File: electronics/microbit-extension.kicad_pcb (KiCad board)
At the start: 2 copper layers, 55.9 x 63.5 mm, 29 parts, among them J1 microbit_edge_connector, SW1 SW_DIP_x01, SW2 SW_DIP_x01, SW3 SW_DIP_x01, SW4 SW_DIP_x01, U1 LD1117S33CTR

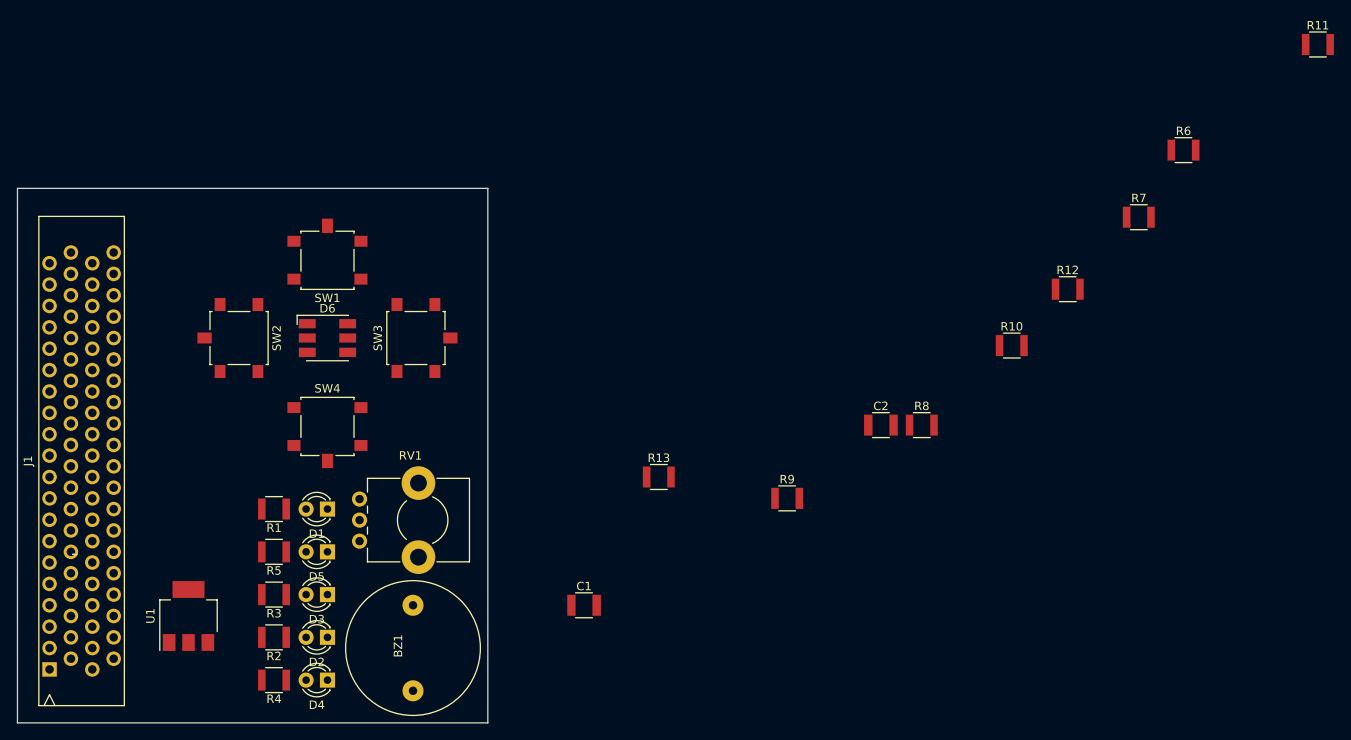
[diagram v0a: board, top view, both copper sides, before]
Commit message: need to redo and check the footprint association
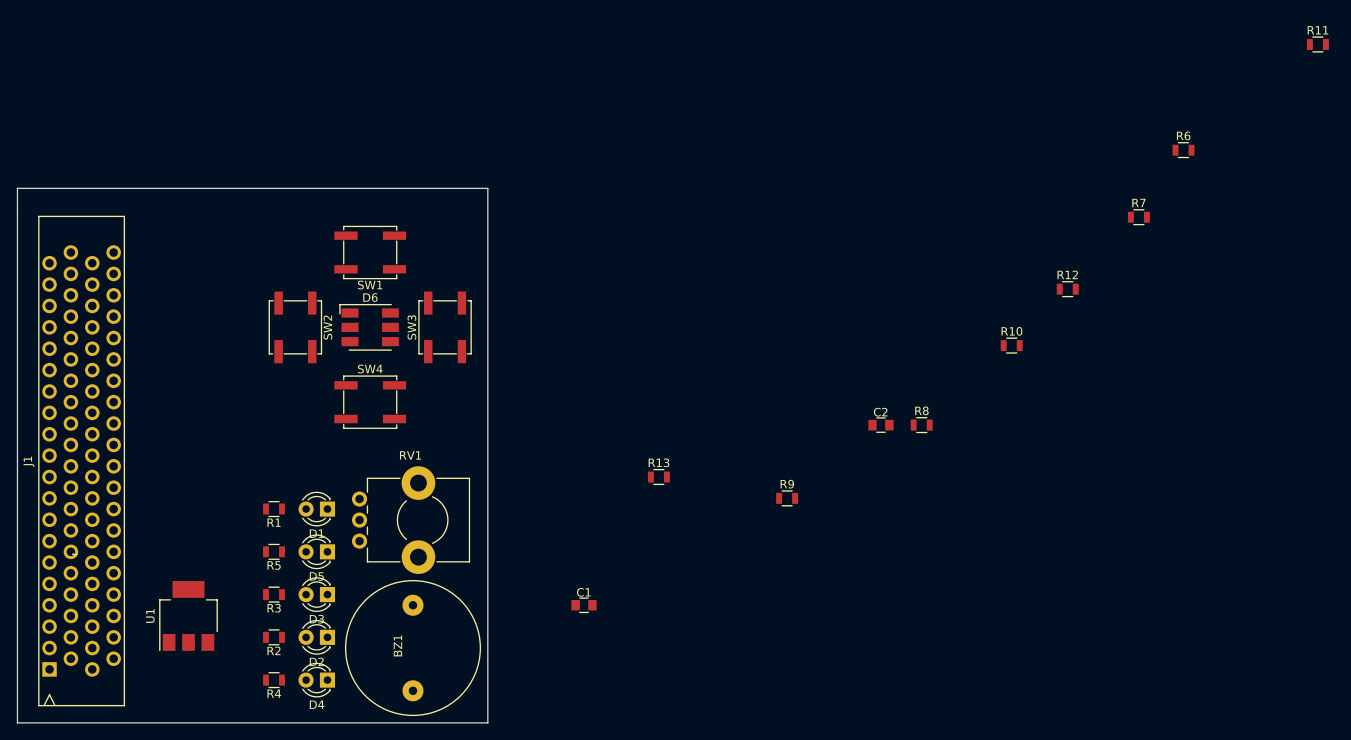
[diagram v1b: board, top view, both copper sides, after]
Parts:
- C1, C2: footprint Capacitors_SMD:C_1210 -> Capacitors_SMD:C_0805
- R1, R10, R11, R12, R13, R2, R3, R4, R5, R6, R7, R8, R9: footprint Resistors_SMD:R_1210 -> Resistors_SMD:R_0805
- SW1, SW2, SW3, SW4: footprint Buttons_Switches_SMD:SW_SPST_B3S-1100 -> Buttons_Switches_SMD:SW_SPST_EVPBF
- moved SW2 7.73 mm to (76.2, 82.5)
- moved SW4 6.35 mm to (85.1, 91.4)
- moved D6 5.24 mm to (85.1, 82.5)
- moved SW1 5.08 mm to (85.1, 73.7)
- moved SW3 2.84 mm to (94.0, 82.5)

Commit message: more layouting
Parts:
- moved U1 53.1 mm to (116.3, 122.4)
- moved D6 14.2 mm to (70.9, 82.5)
- moved SW1 14.2 mm to (70.9, 73.7)
- moved SW2 14.2 mm to (62.0, 82.5)
- moved SW3 14.2 mm to (79.8, 82.5)
- moved SW4 14.2 mm to (70.9, 91.4)
- moved D1 13.3 mm to (66.8, 103.0)
- moved D2 13.3 mm to (66.8, 118.2)
- moved D3 13.3 mm to (66.8, 113.2)
- moved D4 13.3 mm to (66.8, 123.3)
- moved D5 13.3 mm to (66.8, 108.1)
- moved R1 13.3 mm to (60.5, 103.0)
- moved R2 13.3 mm to (60.5, 118.2)
- moved R3 13.3 mm to (60.5, 113.2)
- moved R4 13.3 mm to (60.5, 123.3)
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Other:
- board size 55.9 x 63.5 mm -> 43.2 x 59.7 mm
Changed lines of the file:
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@@
     (links 78)
     (no_connects 78)
-    (area 43.104999 65.964999 99.135001 129.615001)
+    (area 43.739999 68.504999 87.070001 128.345001)
     (thickness 1.6)
     (drawings 5)
@@
   )
   (module Buzzers_Beepers:BUZZER (layer F.Cu)
-    (at 90.17 120.65 90)
+    (at 78.74 120.015 90)
     (fp_text reference BZ1 (at 0.24892 -1.75006 90) (layer F.SilkS)
       (effects (font (size 1 1) (thickness 0.15)))
@@
   )
   (module LEDs:LED_D3.0mm (layer F.Cu)
-    (at 80.01 104.14 180)
+    (at 66.802 102.997 180)
     (descr "LED, diameter 3.0mm, 2 pins")
     (tags "LED diameter 3.0mm 2 pins")
@@
   )
   (module LEDs:LED_D3.0mm (layer F.Cu)
-    (at 80.01 119.38 180)
+    (at 66.802 118.237 180)
     (descr "LED, diameter 3.0mm, 2 pins")
     (tags "LED diameter 3.0mm 2 pins")
@@
   )
   (module LEDs:LED_D3.0mm (layer F.Cu)
-    (at 80.01 114.3 180)
+    (at 66.802 113.157 180)
     (descr "LED, diameter 3.0mm, 2 pins")
     (tags "LED diameter 3.0mm 2 pins")
@@
   )
   (module LEDs:LED_D3.0mm (layer F.Cu)
-    (at 80.01 124.46 180)
+    (at 66.802 123.317 180)
     (descr "LED, diameter 3.0mm, 2 pins")
     (tags "LED diameter 3.0mm 2 pins")
@@
   )
   (module LEDs:LED_D3.0mm (layer F.Cu)
-    (at 80.01 109.22 180)
+    (at 66.802 108.077 180)
     (descr "LED, diameter 3.0mm, 2 pins")
     (tags "LED diameter 3.0mm 2 pins")
@@
   )
   (module LEDs:LED_RGB_5050-6 (layer F.Cu)
-    (at 85.09 82.55)
+    (at 70.866 82.55)
     (descr http://cdn.sparkfun.com/datasheets/Components/LED/5060BRG4.pdf)
     (tags "RGB LED 5050-6")
@@
   )
   (module Potentiometers:Potentiometer_Alps_RK09K_Horizontal (layer F.Cu)
-    (at 83.82 107.95)
+    (at 85.09 102.235 180)
     (descr "Potentiometer, horizontally mounted, Omeg PC16PU, Omeg PC16PU, Omeg PC16PU, Vishay/Spectrol 248GJ/249GJ Single, Vishay/Spectrol 248GJ/249GJ Single, Vishay/Spectrol 248GJ/249GJ Single, Vishay/Spectrol 248GH/249GH Single, Vishay/Spectrol 148/149 Single, Vishay/Spectrol 148/149 Single, Vishay/Spectrol 148/149 Single, Vishay/Spectrol 148A/149A Single with mounting plates, Vishay/Spectrol 148/149 Double, Vishay/Spectrol 148A/149A Double with mounting plates, Piher PC-16 Single, Piher PC-16 Single, Piher PC-16 Single, Piher PC-16SV Single, Piher PC-16 Double, Piher PC-16 Triple, Piher T16H Single, Piher T16L Single, Piher T16H Double, Alps RK163 Single, Alps RK163 Double, Alps RK097 Single, Alps RK097 Double, Bourns PTV09A-2 Single with mounting sleve Single, Bourns PTV09A-1 with mounting sleve Single, Bourns PRS11S Single, Alps RK09K Single with mounting sleve Single, Alps RK09K with mounting sleve Single, http://www.alps.com/prod/info/E/HTML/Potentiometer/RotaryPotentiometers/RK09K/RK09D1130C1B.html")
     (tags "Potentiometer horizontal  Omeg PC16PU  Omeg PC16PU  Omeg PC16PU  Vishay/Spectrol 248GJ/249GJ Single  Vishay/Spectrol 248GJ/249GJ Single  Vishay/Spectrol 248GJ/249GJ Single  Vishay/Spectrol 248GH/249GH Single  Vishay/Spectrol 148/149 Single  Vishay/Spectrol 148/149 Single  Vishay/Spectrol 148/149 Single  Vishay/Spectrol 148A/149A Single with mounting plates  Vishay/Spectrol 148/149 Double  Vishay/Spectrol 148A/149A Double with mounting plates  Piher PC-16 Single  Piher PC-16 Single  Piher PC-16 Single  Piher PC-16SV Single  Piher PC-16 Double  Piher PC-16 Triple  Piher T16H Single  Piher T16L Single  Piher T16H Double  Alps RK163 Single  Alps RK163 Double  Alps RK097 Single  Alps RK097 Double  Bourns PTV09A-2 Single with mounting sleve Single  Bourns PTV09A-1 with mounting sleve Single  Bourns PRS11S Single  Alps RK09K Single with mounting sleve Single  Alps RK09K with mounting sleve Single")
-    (fp_text reference RV1 (at 6.05 -10.15) (layer F.SilkS)
-      (effects (font (size 1 1) (thickness 0.15)))
-    )
-    (fp_text value POT (at 6.05 5.15) (layer F.Fab)
+    (fp_text reference RV1 (at 6.05 -10.15 180) (layer F.SilkS)
+      (effects (font (size 1 1) (thickness 0.15)))
+    )
+    (fp_text value POT (at 6.05 5.15 180) (layer F.Fab)
       (effects (font (size 1 1) (thickness 0.15)))
     )
@@
     (fp_line (start 13.25 4.15) (end 13.25 -9.15) (layer F.CrtYd) (width 0.05))
     (fp_line (start 13.25 -9.15) (end -1.15 -9.15) (layer F.CrtYd) (width 0.05))
-    (pad 3 thru_hole circle (at 0 -5) (size 1.8 1.8) (drill 1) (layers *.Cu *.Mask)
+    (pad 3 thru_hole circle (at 0 -5 180) (size 1.8 1.8) (drill 1) (layers *.Cu *.Mask)
       (net 2 +3V3))
-    (pad 2 thru_hole circle (at 0 -2.5) (size 1.8 1.8) (drill 1) (layers *.Cu *.Mask)
+    (pad 2 thru_hole circle (at 0 -2.5 180) (size 1.8 1.8) (drill 1) (layers *.Cu *.Mask)
       (net 37 /AI0))
-    (pad 1 thru_hole circle (at 0 0) (size 1.8 1.8) (drill 1) (layers *.Cu *.Mask)
-      (net 4 GND))
-    (pad 0 np_thru_hole circle (at 7 -6.9) (size 4 4) (drill 2) (layers *.Cu *.Mask))
-    (pad 0 np_thru_hole circle (at 7 1.9) (size 4 4) (drill 2) (layers *.Cu *.Mask))
+    (pad 1 thru_hole circle (at 0 0 180) (size 1.8 1.8) (drill 1) (layers *.Cu *.Mask)
+      (net 4 GND))
+    (pad 0 np_thru_hole circle (at 7 -6.9 180) (size 4 4) (drill 2) (layers *.Cu *.Mask))
+    (pad 0 np_thru_hole circle (at 7 1.9 180) (size 4 4) (drill 2) (layers *.Cu *.Mask))
     (model Potentiometers.3dshapes/Potentiometer_Alps_RK09K_Horizontal.wrl
       (at (xyz 0 0 0))
@@
   )
   (module TO_SOT_Packages_SMD:SOT-223 (layer F.Cu)
-    (at 63.5 116.84 90)
+    (at 116.332 122.428 90)
     (descr "module CMS SOT223 4 pins")
     (tags "CMS SOT")
@@
   )
   (module Resistors_SMD:R_0805 (layer F.Cu)
-    (at 73.66 104.14 180)
+    (at 60.452 102.997 180)
     (descr "Resistor SMD 0805, reflow soldering, Vishay (see dcrcw.pdf)")
     (tags "resistor 0805")
@@
   )
   (module Resistors_SMD:R_0805 (layer F.Cu)
-    (at 73.66 119.38 180)
+    (at 60.452 118.237 180)
     (descr "Resistor SMD 0805, reflow soldering, Vishay (see dcrcw.pdf)")
     (tags "resistor 0805")
@@
   )
   (module Resistors_SMD:R_0805 (layer F.Cu)
-    (at 73.66 114.3 180)
+    (at 60.452 113.157 180)
     (descr "Resistor SMD 0805, reflow soldering, Vishay (see dcrcw.pdf)")
     (tags "resistor 0805")
@@
   )
   (module Resistors_SMD:R_0805 (layer F.Cu)
-    (at 73.66 124.46 180)
+    (at 60.452 123.317 180)
     (descr "Resistor SMD 0805, reflow soldering, Vishay (see dcrcw.pdf)")
     (tags "resistor 0805")
@@
   )
   (module Resistors_SMD:R_0805 (layer F.Cu)
-    (at 73.66 109.22 180)
+    (at 60.452 108.077 180)
     (descr "Resistor SMD 0805, reflow soldering, Vishay (see dcrcw.pdf)")
     (tags "resistor 0805")
@@
   )
   (module Buttons_Switches_SMD:SW_SPST_EVPBF (layer F.Cu)
-    (at 85.09 73.66 180)
+    (at 70.866 73.66 180)
     (descr "Light Touch Switch")
     (attr smd)
@@
   )
   (module Buttons_Switches_SMD:SW_SPST_EVPBF (layer F.Cu)
-    (at 76.2 82.55 270)
+    (at 61.976 82.55 270)
     (descr "Light Touch Switch")
     (attr smd)
@@
   )
   (module Buttons_Switches_SMD:SW_SPST_EVPBF (layer F.Cu)
-    (at 93.98 82.55 90)
+    (at 79.756 82.55 90)
     (descr "Light Touch Switch")
     (attr smd)
@@
   )
   (module Buttons_Switches_SMD:SW_SPST_EVPBF (layer F.Cu)
-    (at 85.09 91.44)
+    (at 70.866 91.44)
     (descr "Light Touch Switch")
     (attr smd)
@@
     )
   )
-  (gr_line (start 43.18 66.04) (end 43.18 68.58) (angle 90) (layer Edge.Cuts) (width 0.15))
-  (gr_line (start 99.06 66.04) (end 43.18 66.04) (angle 90) (layer Edge.Cuts) (width 0.15))
-  (gr_line (start 99.06 129.54) (end 99.06 66.04) (angle 90) (layer Edge.Cuts) (width 0.15))
-  (gr_line (start 43.18 129.54) (end 99.06 129.54) (angle 90) (layer Edge.Cuts) (width 0.15))
-  (gr_line (start 43.18 68.58) (end 43.18 129.54) (angle 90) (layer Edge.Cuts) (width 0.15))
+  (gr_line (start 44.45 68.58) (end 43.815 68.58) (angle 90) (layer Edge.Cuts) (width 0.15))
+  (gr_line (start 44.45 128.27) (end 44.45 68.58) (angle 90) (layer Edge.Cuts) (width 0.15))
+  (gr_line (start 86.995 128.27) (end 44.45 128.27) (angle 90) (layer Edge.Cuts) (width 0.15))
+  (gr_line (start 86.995 68.58) (end 86.995 128.27) (angle 90) (layer Edge.Cuts) (width 0.15))
+  (gr_line (start 44.45 68.58) (end 86.995 68.58) (angle 90) (layer Edge.Cuts) (width 0.15))
 )

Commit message: more layout planning
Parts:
- moved R11 121.1 mm to (79.8, 76.5)
- moved R6 120.1 mm to (62.0, 70.4), turned to 180 degrees
- moved R7 114.5 mm to (62.0, 72.3), turned to 180 degrees
- moved R8 90.9 mm to (62.0, 74.2), turned to 180 degrees
- moved R12 88.4 mm to (79.8, 72.4), turned to 180 degrees
- moved R10 82.8 mm to (79.8, 70.4), turned to 180 degrees
- moved R9 77.5 mm to (62.0, 75.9)
- moved R13 47.3 mm to (79.8, 74.4), turned to 180 degrees
- moved C2 37.4 mm to (110.8, 107.5)
- moved C1 10.9 mm to (99.7, 116.8)
- moved U1 10.9 mm to (105.5, 123.7)

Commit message: a bit more routing work
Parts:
- moved U1 34.3 mm to (104.9, 89.4)
- moved R11 5.84 mm to (79.8, 70.6), turned to 180 degrees
- moved R10 3.81 mm to (79.8, 74.2)
- moved R12 3.56 mm to (79.8, 75.9)
- moved R13 2.03 mm to (79.8, 72.4)
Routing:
- net GND: track 0.00 -> 56.8 mm
- net /RGBB: track 0.00 -> 32.0 mm, vias 0 -> 2
- net /SW2: track 0.00 -> 31.3 mm, vias 0 -> 2
- net /SW4: track 0.00 -> 27.1 mm, vias 0 -> 2
- net /RGBG: track 0.00 -> 26.9 mm
- net +3V3: track 0.00 -> 25.4 mm
- net Net-(D6-Pad4): track 0.00 -> 24.8 mm
- net /RGBR: track 0.00 -> 24.0 mm
- net Net-(D6-Pad5): track 0.00 -> 21.1 mm
- net Net-(D6-Pad6): track 0.00 -> 14.3 mm
- net /SW1: track 0.00 -> 11.4 mm
- net /SW3: track 0.00 -> 10.3 mm
- net /AI2: track 0.00 -> 8.15 mm
- net /AI1: track 0.00 -> 8.15 mm
- net /AI0: track 0.00 -> 8.15 mm
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
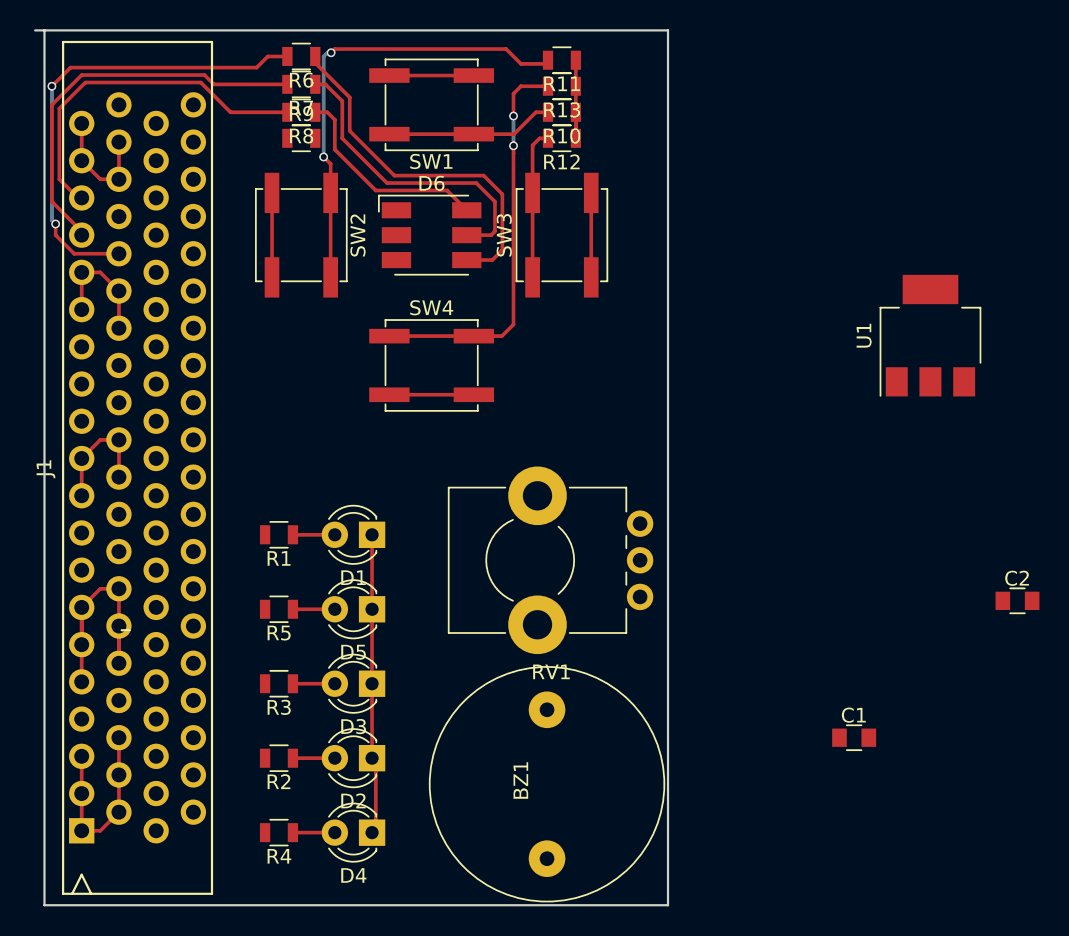
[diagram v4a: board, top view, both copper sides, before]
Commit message: routing is more complete
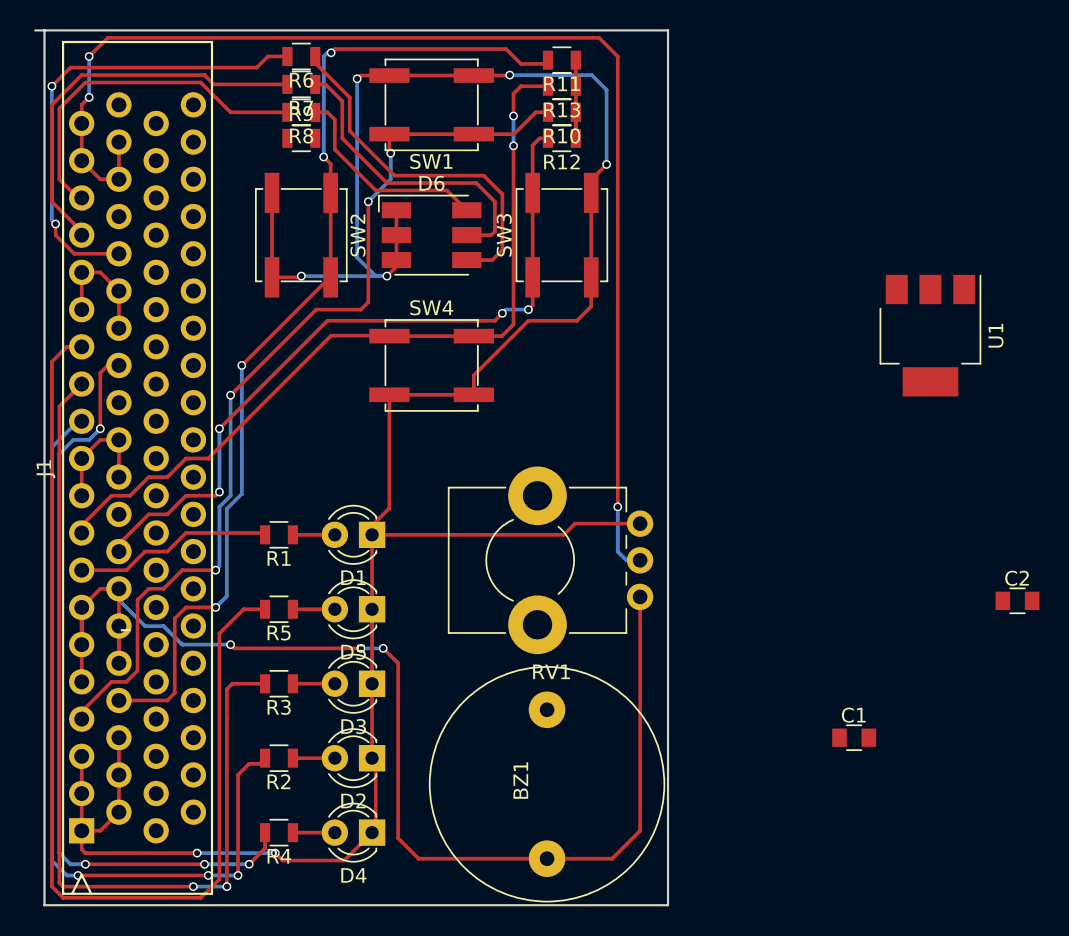
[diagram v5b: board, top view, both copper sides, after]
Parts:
- turned U1 to 270 degrees
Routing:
- net GND: track 56.8 -> 167.5 mm, vias 0 -> 7
- net /AI0: track 8.15 -> 85.6 mm, vias 0 -> 3
- net /LED4: track 0.00 -> 71.1 mm
- net +3V3: track 25.4 -> 92.8 mm, vias 0 -> 3
- net /LED2: track 0.00 -> 62.4 mm, vias 0 -> 2
- net /LED1: track 0.00 -> 53.3 mm, vias 0 -> 3
- net /SW1: track 11.4 -> 64.4 mm, vias 0 -> 4
- net /LED3: track 0.00 -> 51.9 mm, vias 0 -> 4
- net /SW3: track 10.3 -> 50.2 mm, vias 0 -> 4
- net /SW2: track 31.3 -> 69.3 mm, vias 2 -> 4
- net /SW4: track 27.1 -> 54.2 mm
- net /LED0: track 0.00 -> 13.6 mm

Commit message: finishing up routing
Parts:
- added J2: 9V conn, Pin_Headers:Pin_Header_Straight_1x02_Pitch2.54mm, F.Cu at (84.8, 73.2)
- added T1: 2N4401, TO_SOT_Packages_SMD:SOT-23, F.Cu at (71.1, 119.6)
- moved C2 39.3 mm to (84.3, 78.5), turned to 270 degrees
- moved C1 32.6 mm to (82.8, 88.9), turned to 180 degrees
- moved U1 24.2 mm to (81.0, 93.5), turned to 180 degrees
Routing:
- net +3V3: track 92.8 -> 131.6 mm, vias 3 -> 7
- net +9V: track 0.00 -> 21.4 mm
- net GND: track 167.5 -> 183.3 mm
- net /AI0: track 85.6 -> 90.6 mm
